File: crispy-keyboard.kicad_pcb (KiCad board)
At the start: 2 copper layers, 331.2 x 124.4 mm, 204 parts, among them J1 AVR-ISP-6, J2 Conn_01x03_Female, Q1 Q_PMOS_DSG, SW1 KEYSW, SW10 KEYSW, SW11 KEYSW, SW12 KEYSW, SW13 KEYSW, SW14 KEYSW, SW15 KEYSW, SW16 KEYSW, SW17 KEYSW, SW18 KEYSW, SW19 KEYSW, SW2 KEYSW, SW20 KEYSW, SW21 KEYSW, SW22 KEYSW, SW23 KEYSW, SW24 KEYSW, SW25 KEYSW, SW26 KEYSW, SW27 KEYSW, SW28 KEYSW, SW29 KEYSW, SW3 KEYSW, SW30 KEYSW, SW31 KEYSW, SW32 KEYSW, SW33 KEYSW, SW34 KEYSW, SW35 KEYSW, SW36 KEYSW, SW37 KEYSW, SW38 KEYSW, SW39 KEYSW, SW4 KEYSW, SW40 KEYSW, SW41 KEYSW, SW42 KEYSW, SW43 KEYSW, SW44 KEYSW, SW45 KEYSW, SW46 KEYSW, SW47 KEYSW, SW48 KEYSW, SW49 KEYSW, SW5 KEYSW, SW50 KEYSW, SW51 KEYSW, SW52 KEYSW, SW53 KEYSW, SW54 KEYSW, SW55 KEYSW, SW56 KEYSW, SW57 KEYSW, SW58 KEYSW, SW59 KEYSW, SW6 KEYSW, SW60 KEYSW, SW61 KEYSW, SW62 KEYSW, SW63 KEYSW, SW64 KEYSW, SW65 KEYSW, SW66 KEYSW, SW67 KEYSW, SW68 KEYSW, SW69 KEYSW, SW7 KEYSW, SW70 KEYSW, SW71 KEYSW, SW72 KEYSW, SW73 KEYSW, SW74 KEYSW, SW75 KEYSW, SW76 KEYSW, SW77 KEYSW, SW78 KEYSW, SW79 KEYSW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

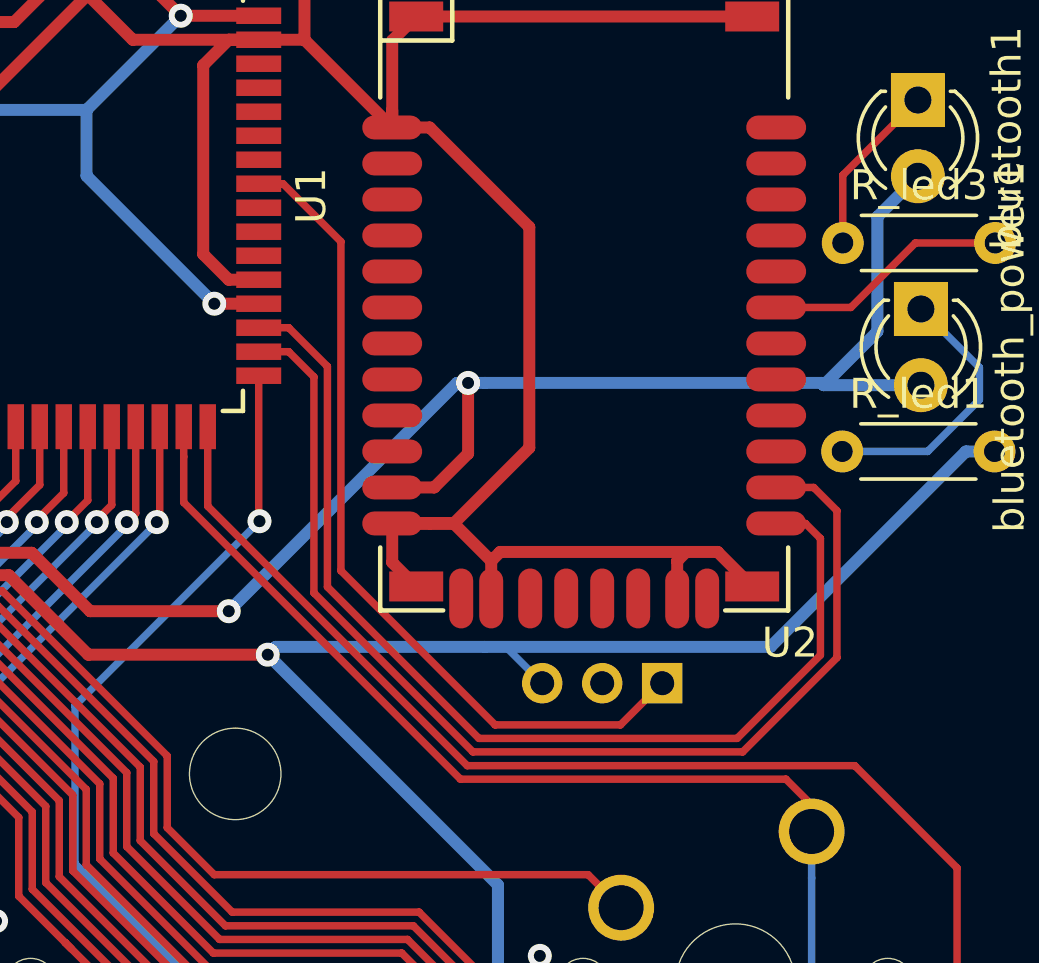
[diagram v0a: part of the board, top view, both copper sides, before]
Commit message: Changed power pin of external RGB LED Strip to POW_5V from USB_POW
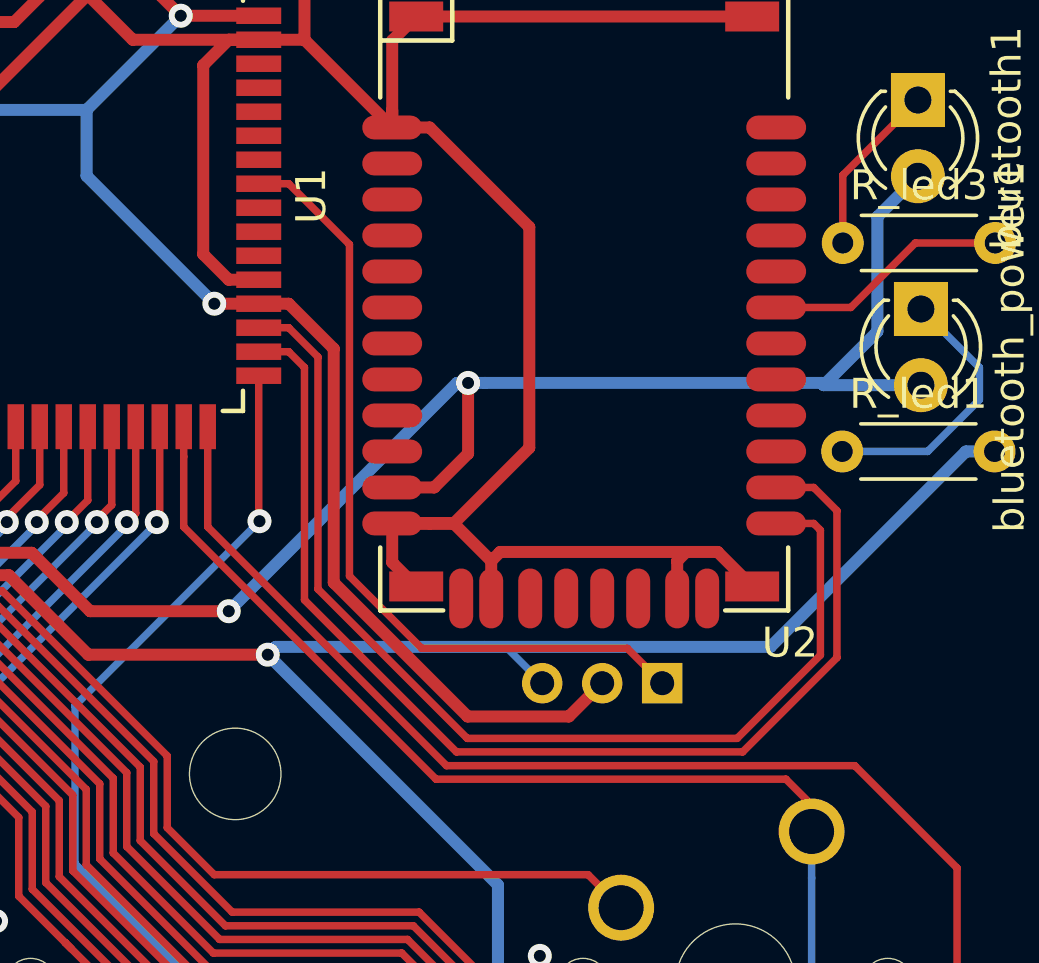
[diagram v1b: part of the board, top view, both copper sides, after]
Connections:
- J2 pad 2: USB_POW -> POW_5V
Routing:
- net POW_5V: track 100.0 -> 122.2 mm
- net RGB_Pin: track 27.9 -> 26.8 mm
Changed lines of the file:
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@@
     (thickness 1.6)
     (drawings 38)
-    (tracks 2497)
+    (tracks 2503)
     (zones 0)
     (modules 204)
@@
       (net 1 GND))
     (pad 2 thru_hole oval (at 0 -2 90) (size 1.35 1.35) (drill 0.8) (layers *.Cu *.Mask)
-      (net 160 USB_POW))
+      (net 147 POW_5V))
     (pad 1 thru_hole rect (at 0 0 90) (size 1.35 1.35) (drill 0.8) (layers *.Cu *.Mask)
       (net 183 RGB_Pin))
@@
   (segment (start 351.63125 146.84375) (end 352.731249 147.943749) (width 0.25) (layer B.Cu) (net 88))
   (segment (start 351.63125 108.74375) (end 352.731249 109.843749) (width 0.25) (layer B.Cu) (net 88))
-  (segment (start 351.63125 89.69375) (end 351.63125 88.80625) (width 0.25) (layer F.Cu) (net 88))
-  (segment (start 351.63125 88.80625) (end 350.775 87.95) (width 0.25) (layer F.Cu) (net 88))
-  (segment (start 339.925 87.95) (end 330.7 78.725) (width 0.25) (layer F.Cu) (net 88))
-  (segment (start 350.775 87.95) (end 339.925 87.95) (width 0.25) (layer F.Cu) (net 88))
-  (segment (start 330.7 78.725) (end 330.7 77.2) (width 0.25) (layer F.Cu) (net 88))
   (segment (start 330.7 77.2) (end 330.7 76.2) (width 0.25) (layer F.Cu) (net 88))
+  (segment (start 330.7 79.54) (end 330.7 77.2) (width 0.25) (layer F.Cu) (net 88))
+  (segment (start 339.11 87.95) (end 330.7 79.54) (width 0.25) (layer F.Cu) (net 88))
+  (segment (start 350.775 87.95) (end 339.11 87.95) (width 0.25) (layer F.Cu) (net 88))
+  (segment (start 351.63125 88.80625) (end 350.775 87.95) (width 0.25) (layer F.Cu) (net 88))
+  (segment (start 351.63125 89.69375) (end 351.63125 88.80625) (width 0.25) (layer F.Cu) (net 88))
   (segment (start 267.275 70.85) (end 267.252297 70.872703) (width 0.25) (layer F.Cu) (net 89))
   (segment (start 300.023159 75.817041) (end 272.196635 75.817041) (width 0.25) (layer B.Cu) (net 89))
@@
   (segment (start 351.14 78.225) (end 350.45 78.225) (width 0.25) (layer F.Cu) (net 118))
   (segment (start 333.2 73.7) (end 334.2 73.7) (width 0.25) (layer F.Cu) (net 118))
-  (segment (start 351.7 78.225) (end 350.45 78.225) (width 0.25) (layer F.Cu) (net 118))
-  (segment (start 352.475 79) (end 351.7 78.225) (width 0.25) (layer F.Cu) (net 118))
+  (segment (start 334.2 73.7) (end 334.724969 74.224969) (width 0.25) (layer F.Cu) (net 118))
+  (segment (start 334.724969 81.974969) (end 339.790011 87.040011) (width 0.25) (layer F.Cu) (net 118))
+  (segment (start 339.790011 87.040011) (end 349.33499 87.040011) (width 0.25) (layer F.Cu) (net 118))
   (segment (start 352.475 83.9) (end 352.475 79) (width 0.25) (layer F.Cu) (net 118))
-  (segment (start 335.04 74.54) (end 335.04 81.74) (width 0.25) (layer F.Cu) (net 118))
-  (segment (start 340.340011 87.040011) (end 349.33499 87.040011) (width 0.25) (layer F.Cu) (net 118))
-  (segment (start 334.2 73.7) (end 335.04 74.54) (width 0.25) (layer F.Cu) (net 118))
+  (segment (start 352.475 79) (end 351.7 78.225) (width 0.25) (layer F.Cu) (net 118))
+  (segment (start 351.7 78.225) (end 350.45 78.225) (width 0.25) (layer F.Cu) (net 118))
   (segment (start 349.33499 87.040011) (end 352.475 83.9) (width 0.25) (layer F.Cu) (net 118))
-  (segment (start 335.04 81.74) (end 340.340011 87.040011) (width 0.25) (layer F.Cu) (net 118))
-  (segment (start 335.490011 81.540011) (end 335.490011 74.190011) (width 0.25) (layer F.Cu) (net 119))
-  (segment (start 335.490011 74.190011) (end 334.2 72.9) (width 0.25) (layer F.Cu) (net 119))
-  (segment (start 340.54 86.59) (end 335.490011 81.540011) (width 0.25) (layer F.Cu) (net 119))
-  (segment (start 351.925 79.925) (end 351.925 83.81359) (width 0.25) (layer F.Cu) (net 119))
-  (segment (start 351.425 79.425) (end 351.925 79.925) (width 0.25) (layer F.Cu) (net 119))
-  (segment (start 350.45 79.425) (end 351.425 79.425) (width 0.25) (layer F.Cu) (net 119))
+  (segment (start 334.724969 74.224969) (end 334.724969 81.974969) (width 0.25) (layer F.Cu) (net 118))
   (segment (start 351.925 83.81359) (end 349.14859 86.59) (width 0.25) (layer F.Cu) (net 119))
+  (segment (start 349.14859 86.59) (end 340.151111 86.59) (width 0.25) (layer F.Cu) (net 119))
+  (segment (start 340.151111 86.59) (end 335.17498 81.613869) (width 0.25) (layer F.Cu) (net 119))
+  (segment (start 335.17498 81.613869) (end 335.17498 73.87498) (width 0.25) (layer F.Cu) (net 119))
+  (segment (start 335.17498 73.87498) (end 334.2 72.9) (width 0.25) (layer F.Cu) (net 119))
+  (segment (start 350.45 79.425) (end 351.7 79.425) (width 0.25) (layer F.Cu) (net 119))
+  (segment (start 351.7 79.425) (end 351.925 79.65) (width 0.25) (layer F.Cu) (net 119))
   (segment (start 334.2 72.9) (end 333.2 72.9) (width 0.25) (layer F.Cu) (net 119))
-  (segment (start 349.14859 86.59) (end 340.54 86.59) (width 0.25) (layer F.Cu) (net 119))
+  (segment (start 351.925 79.65) (end 351.925 83.81359) (width 0.25) (layer F.Cu) (net 119))
   (segment (start 329.9 61.8) (end 329.9 60.8) (width 0.4) (layer F.Cu) (net 147))
   (segment (start 330.6 62.5) (end 329.9 61.8) (width 0.4) (layer F.Cu) (net 147))
@@
   (segment (start 294.357838 70.4) (end 288.65001 70.4) (width 0.4) (layer F.Cu) (net 147))
   (segment (start 295.584138 69.1737) (end 294.357838 70.4) (width 0.4) (layer F.Cu) (net 147))
+  (segment (start 334.2 72.1) (end 333.2 72.1) (width 0.4) (layer F.Cu) (net 147))
+  (segment (start 340.163588 85.86) (end 335.699991 81.396403) (width 0.4) (layer F.Cu) (net 147))
+  (segment (start 335.699991 73.599991) (end 334.2 72.1) (width 0.4) (layer F.Cu) (net 147))
+  (segment (start 343.54 85.86) (end 340.163588 85.86) (width 0.4) (layer F.Cu) (net 147))
+  (segment (start 344.65 84.75) (end 343.54 85.86) (width 0.4) (layer F.Cu) (net 147))
+  (segment (start 335.699991 81.396403) (end 335.699991 73.599991) (width 0.4) (layer F.Cu) (net 147))
   (segment (start 270.75 72) (end 270.775 71.975) (width 0.25) (layer F.Cu) (net 148))
   (segment (start 270.775 73.725) (end 270.725 73.775) (width 0.25) (layer F.Cu) (net 148))
@@
   (segment (start 40.89 146.82) (end 40.89 127.775) (width 0.25) (layer B.Cu) (net 163))
   (segment (start 40.89 127.775) (end 40.89 108.72) (width 0.25) (layer B.Cu) (net 163))
-  (segment (start 347.315998 176.09) (end 51.12 176.09) (width 0.25) (layer F.Cu) (net 163))
-  (segment (start 331.5 78.85) (end 340.149989 87.499989) (width 0.25) (layer F.Cu) (net 163))
-  (segment (start 340.149989 87.499989) (end 353.069989 87.499989) (width 0.25) (layer F.Cu) (net 163))
   (segment (start 356.48 166.925998) (end 347.315998 176.09) (width 0.25) (layer F.Cu) (net 163))
   (segment (start 356.48 90.91) (end 356.48 166.925998) (width 0.25) (layer F.Cu) (net 163))
-  (segment (start 331.5 76.2) (end 331.5 78.85) (width 0.25) (layer F.Cu) (net 163))
   (segment (start 51.12 176.09) (end 40.89 165.86) (width 0.25) (layer F.Cu) (net 163))
   (segment (start 353.069989 87.499989) (end 356.48 90.91) (width 0.25) (layer F.Cu) (net 163))
+  (segment (start 339.459989 87.499989) (end 353.069989 87.499989) (width 0.25) (layer F.Cu) (net 163))
+  (segment (start 331.5 79.54) (end 339.459989 87.499989) (width 0.25) (layer F.Cu) (net 163))
+  (segment (start 347.315998 176.09) (end 51.12 176.09) (width 0.25) (layer F.Cu) (net 163))
+  (segment (start 331.5 76.2) (end 331.5 79.54) (width 0.25) (layer F.Cu) (net 163))
   (via (at 333.225 79.35) (size 0.8) (drill 0.4) (layers F.Cu B.Cu) (net 164))
   (segment (start 337.6114 94.39999) (end 340.72501 97.5136) (width 0.25) (layer B.Cu) (net 164))
@@
   (segment (start 326.7 59.95388) (end 325.74712 59.001) (width 0.25) (layer F.Cu) (net 178))
   (segment (start 326.7 60.8) (end 326.7 59.95388) (width 0.25) (layer F.Cu) (net 178))
-  (segment (start 345.26001 86.13999) (end 341.079988 86.13999) (width 0.25) (layer F.Cu) (net 183))
-  (segment (start 341.079988 86.13999) (end 335.940021 81.000023) (width 0.25) (layer F.Cu) (net 183))
-  (segment (start 334.010002 68.1) (end 333.2 68.1) (width 0.25) (layer F.Cu) (net 183))
-  (segment (start 346.65 84.75) (end 345.26001 86.13999) (width 0.25) (layer F.Cu) (net 183))
-  (segment (start 335.940021 70.030019) (end 334.010002 68.1) (width 0.25) (layer F.Cu) (net 183))
-  (segment (start 335.940021 81.000023) (end 335.940021 70.030019) (width 0.25) (layer F.Cu) (net 183))
+  (segment (start 346.65 84.75) (end 345.49 83.59) (width 0.25) (layer F.Cu) (net 183))
+  (segment (start 336.225002 70.125002) (end 334.2 68.1) (width 0.25) (layer F.Cu) (net 183))
+  (segment (start 336.225002 81.178938) (end 336.225002 70.125002) (width 0.25) (layer F.Cu) (net 183))
+  (segment (start 345.49 83.59) (end 338.636064 83.59) (width 0.25) (layer F.Cu) (net 183))
+  (segment (start 338.636064 83.59) (end 336.225002 81.178938) (width 0.25) (layer F.Cu) (net 183))
+  (segment (start 334.2 68.1) (end 333.2 68.1) (width 0.25) (layer F.Cu) (net 183))
   (zone (net 1) (net_name GND) (layer F.Cu) (hatch edge 0.508)
     (connect_pads (clearance 0.508))

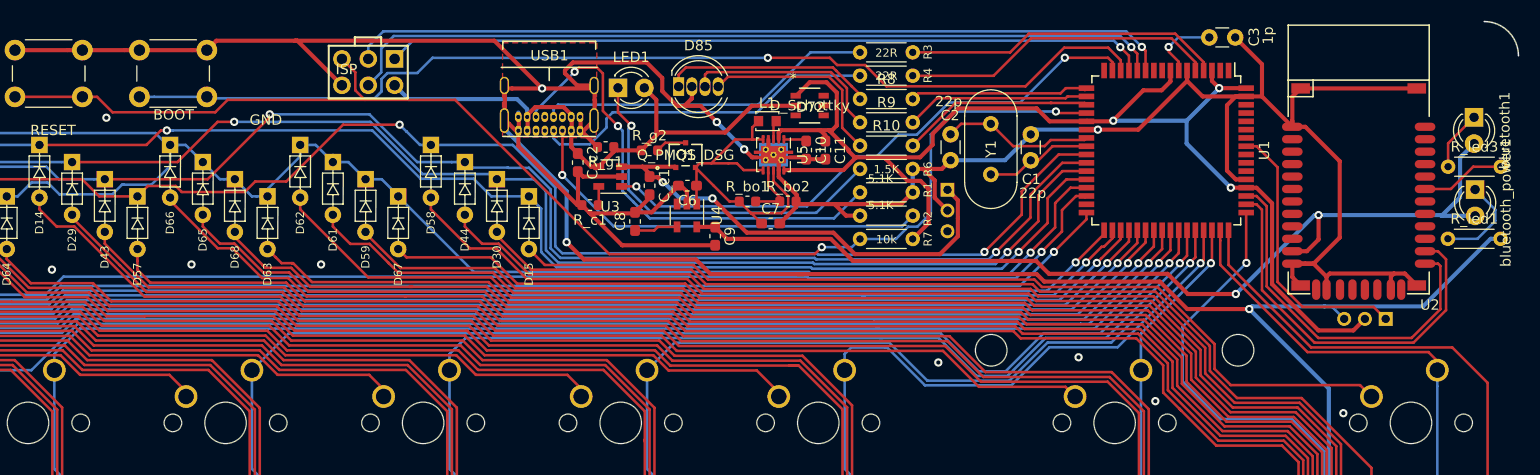
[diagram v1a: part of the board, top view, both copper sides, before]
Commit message: Connected both USB D+ D-
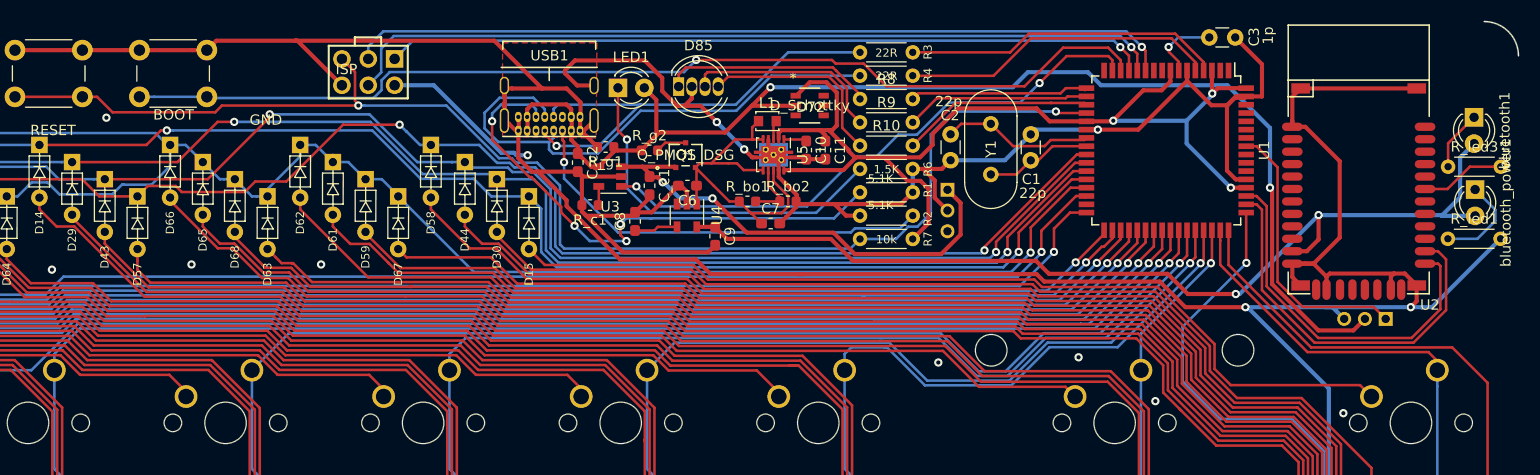
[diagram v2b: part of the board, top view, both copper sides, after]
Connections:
- J2 pad 2: POW_5V -> USB_POW
- R_g2 pad 1: Net-(R_g2-Pad1) -> USB_POW
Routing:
- net USB_POW: track 55.5 -> 137.9 mm, vias 0 -> 3
- net POW_5V: track 122.2 -> 100.3 mm
- net Net-(R4-Pad2): track 34.2 -> 51.6 mm
- net Net-(R3-Pad2): track 33.0 -> 44.8 mm, vias 0 -> 1
- net GND: track 914.5 -> 904.1 mm, vias 36 -> 35
- net Net-(R2-Pad1): track 46.7 -> 52.2 mm, vias 2 -> 4
- net reset: track 125.7 -> 128.4 mm
- net row3: track 410.6 -> 409.4 mm
- net Net-(SW83-PadB): track 293.4 -> 294.3 mm
- net row2: track 294.6 -> 293.7 mm
- net row1: track 292.7 -> 292.0 mm
- net Net-(R1-Pad2): track 40.6 -> 41.1 mm

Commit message: Added PCB edges, swapped USB-C footprint
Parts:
- USB1: footprint crispy:USB_C_GCT_USB4085 -> crispy:GCT_USB4085-GF-A_REVA
- moved USB1 1.14 mm to (264.9, 60.8)
- moved D75 0.36 mm to (49.0, 71.6)
- moved D73 0.35 mm to (45.9, 70.0)
- moved D76 0.21 mm to (39.4, 66.7)
- moved D74 0.19 mm to (42.7, 68.4)
- moved L1 0.08 mm to (287.0, 65.6)
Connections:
- R_g2 pad 1: USB_POW -> Net-(R_g2-Pad1)
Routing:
- net GND: track 904.1 -> 886.3 mm
- net Net-(R4-Pad2): track 51.6 -> 35.6 mm
- net Net-(R3-Pad2): track 44.8 -> 35.7 mm, vias 1 -> 0
- net Net-(R2-Pad1): track 52.2 -> 45.4 mm, vias 4 -> 2
- net Net-(R1-Pad2): track 41.1 -> 43.4 mm
- net Net-(C6-Pad1): track 35.1 -> 33.0 mm
- net USB_POW: track 137.9 -> 137.0 mm, vias 3 -> 2
- net row2: track 293.7 -> 294.3 mm
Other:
- board size 331.2 x 124.4 mm -> 329.9 x 124.6 mm
